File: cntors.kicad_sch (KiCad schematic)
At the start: 11 parts, among them J2 LP-XDS110_Debug_Conn, J3 UART_debug, J4 BAT_JST, J5 JST_conn_2Pi, J7 SOP2_pins, SW2 RST_BUTTON

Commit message: finding exact crystal used in ref design, finishing shcematics
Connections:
- net AWR_TDO is gone; now on net AWR_TDO_SOP0: J2.7 (Pin_7)
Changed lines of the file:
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@@
     )
   )
-  (global_label "AWR_TDO" (shape input) (at 54.61 57.15 180) (fields_autoplaced)
+  (global_label "AWR_TDO_SOP0" (shape input) (at 54.61 57.15 180) (fields_autoplaced)
     (effects (font (size 1 1)) (justify right))
-    (property "Intersheetrefs" "${INTERSHEET_REFS}" (at 45.6883 57.15 0)
+    (property "Intersheetrefs" "${INTERSHEET_REFS}" (at 40.974 57.15 0)
       (effects (font (size 1.27 1.27)) (justify right) hide)
     )

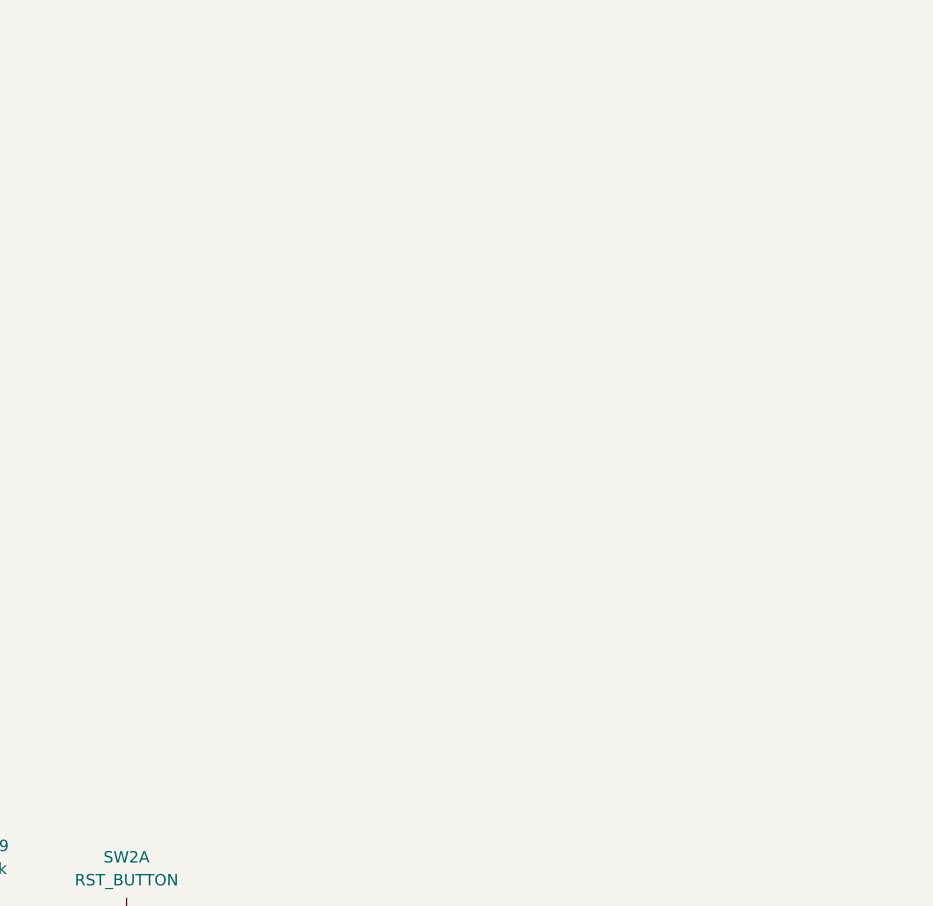
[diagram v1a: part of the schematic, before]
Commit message: adding footprints
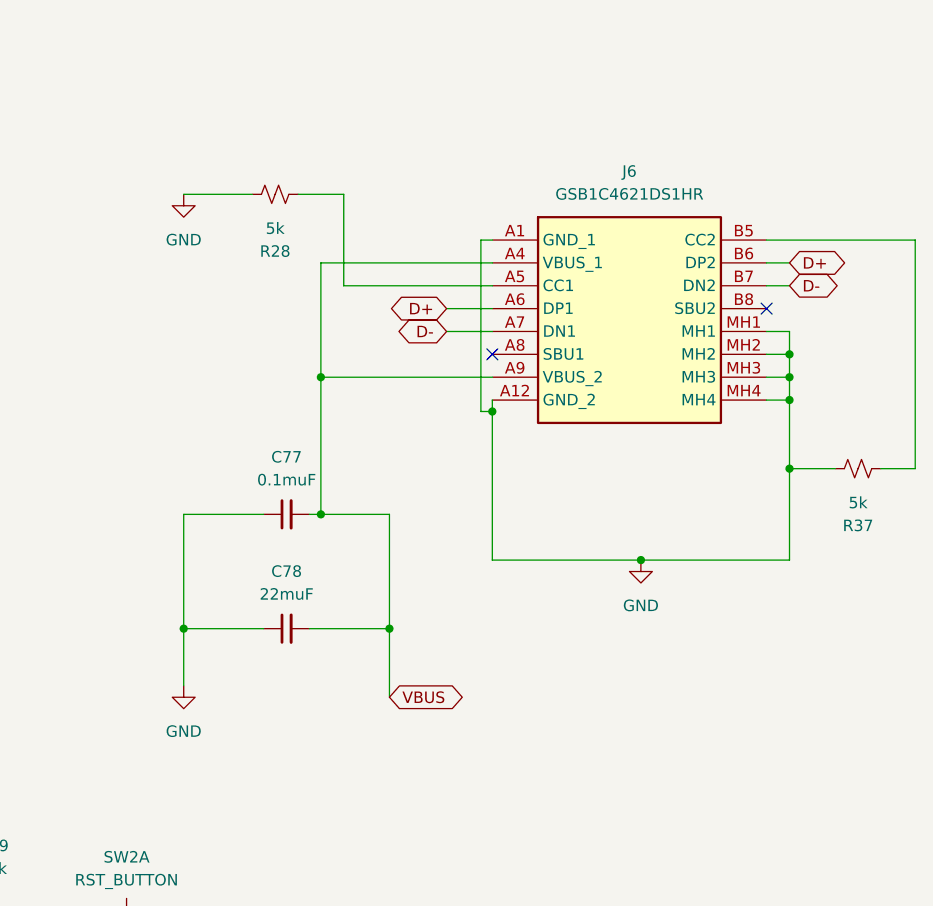
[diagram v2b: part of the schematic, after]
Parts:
- added C77: 0.1muF, Capacitor_SMD:C_0603_1608Metric, symbol Device:C_Small
- added C78: 22muF, Capacitor_SMD:C_0603_1608Metric, symbol Device:C_Small
- added J6: GSB1C4621DS1HR, USB_C2:GSB, symbol USB_C:GSB1C4621DS1HR
- added R28, R37: 5k, Resistor_SMD:R_0603_1608Metric, symbol Device:R_Small_US
- J2: footprint (none) -> XDS_CONN:xds_conn
- J3: footprint (none) -> Connector_PinHeader_2.54mm:PinHeader_1x04_P2.54mm_Vertical
- J4: footprint (none) -> Connector_PinHeader_2.00mm:PinHeader_1x02_P2.00mm_Horizontal
- J5: footprint (none) -> Connector_PinHeader_2.54mm:PinHeader_1x06_P2.54mm_Vertical
- J7: footprint (none) -> Connector_PinHeader_2.54mm:PinHeader_1x03_P2.54mm_Vertical
- R22, R24, R25, R29: footprint (none) -> Resistor_SMD:R_0603_1608Metric
- SW2: footprint (none) -> Inductor_SMD:L_0603_1608Metric
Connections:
- net GND: now also C77.1, C78.1, J6.A1 (GND_1), J6.A12 (GND_2), J6.MH1, J6.MH2, J6.MH3, J6.MH4, R28.2, R37.2
- new net: J6.B5 (CC2), R37.1
- new net: J6.A5 (CC1), R28.1
- new net D+: J6.A6 (DP1), J6.B6 (DP2)
- new net D-: J6.A7 (DN1), J6.B7 (DN2)
- new net VBUS: C77.2, C78.2, J6.A4 (VBUS_1), J6.A9 (VBUS_2)
- no-connect marks 7 -> 9
